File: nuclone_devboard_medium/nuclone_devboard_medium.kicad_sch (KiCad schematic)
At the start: 36 parts, among them J1 JTAG_2X05, J2 TYPE-C-31-M-12, J3 nuclone_medium_left, J4 nuclone_medium_right, SW1 RESET, SW2 Bootloader, U1 MCP1702-MB, U2 TPESD0504C6

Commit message: renamed a library
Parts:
- R1, R13, R2, R3, R4, R5, R6, R7, R8: footprint SquantorRcl:R_0402_hand -> SquantorResistors:R_0402_hand

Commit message: moved RLC parts to different libraries, fixed DRC errors, minor silk movements
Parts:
- added C5: 10n, SquantorCapacitor:C_0402, symbol Device:C
- added R9: 470, SquantorResistor:R_0402_hand, symbol Device:R
- C1, C17, C2: footprint SquantorRcl:C_0603 -> SquantorCapacitor:C_0603
- C14, C4: footprint SquantorRcl:C_0402 -> SquantorCapacitor:C_0402
- C9: footprint SquantorRcl:C_0805 -> SquantorCapacitor:C_0805
- F1: footprint SquantorRcl:F_0603_hand -> SquantorFuse:F_0603_hand
- FB1: footprint SquantorRcl:L_0603 -> SquantorInductor:L_0603
- J2: footprint SquantorUsb:USB-C-HRO-31-M-12 -> SquantorUsb:USB-C-HRO-31-M-12_aisler
- R1, R13, R2, R3, R4, R5, R6, R7, R8: footprint SquantorResistors:R_0402_hand -> SquantorResistor:R_0402_hand
- R14: footprint SquantorRcl:R_0402_hand -> SquantorResistor:R_0402_hand
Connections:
- net VUSB is gone; now on net VBUS: C4.1, U2.5 (VDD)
- net Bootloader: now also C5.1, R9.1; no longer SW2.2
- net DN: now also J2.A7 (DN1), J2.B7 (DN2)
- net DP: now also J2.A6 (DP1), J2.B6 (DP2)
- net VSS: now also C5.2
- new net: R9.2, SW2.2
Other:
- moved on the sheet: SW2

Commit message: updated all footprints, routed and placed, fixed DRC/ERC
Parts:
- C14, C5: value 10n -> 100n; footprint SquantorCapacitor:C_0402 -> SquantorCapacitor:C_0603
- C4: footprint SquantorCapacitor:C_0402 -> SquantorCapacitor:C_0603
- FB1: symbol Device:Ferrite_Bead -> Device:FerriteBead
- N2: value 20211121 -> 20240107
- N5: value Nuclone Template 20211121 -> Nuclone Template 20240107
- R1, R14, R2, R3, R4, R5, R6, R7, R8, R9: footprint SquantorResistor:R_0402_hand -> SquantorResistor:R_0603_hand
- R13: value 100 -> 470; footprint SquantorResistor:R_0402_hand -> SquantorResistor:R_0603_hand
- U1: value MCP1702-MB -> MCP1702-3.3V
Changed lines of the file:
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@@
     )
   )
-  (symbol (lib_id "Device:Ferrite_Bead") (at 63.5 90.17 270) (unit 1)
+  (symbol (lib_id "Device:FerriteBead") (at 63.5 90.17 270) (unit 1)
     (in_bom yes) (on_board yes) (dnp no)
     (property "Reference" "FB1" (at 60.96 87.63 90)
@@
       (effects (font (size 1.524 1.524)) (justify left))
     )
-    (property "Value" "20211121" (at 17.78 182.88 0)
+    (property "Value" "20240107" (at 17.78 182.88 0)
       (effects (font (size 1.524 1.524)) (justify left))
     )
@@
       (effects (font (size 1.524 1.524)))
     )
-    (property "Value" "MCP1702-MB" (at 76.2 181.61 0)
+    (property "Value" "MCP1702-3.3V" (at 76.2 181.61 0)
       (effects (font (size 1.524 1.524)))
     )
@@
       (effects (font (size 1.27 1.27)))
     )
-    (property "Footprint" "SquantorResistor:R_0402_hand" (at 45.72 108.712 90)
+    (property "Footprint" "SquantorResistor:R_0603_hand" (at 45.72 108.712 90)
       (effects (font (size 1.27 1.27)) hide)
     )
@@
       (effects (font (size 1.27 1.27)))
     )
-    (property "Footprint" "SquantorResistor:R_0402_hand" (at 25.4 132.842 90)
+    (property "Footprint" "SquantorResistor:R_0603_hand" (at 25.4 132.842 90)
       (effects (font (size 1.27 1.27)) hide)
     )
@@
       (effects (font (size 1.27 1.27)))
     )
-    (property "Footprint" "SquantorResistor:R_0402_hand" (at 25.4 135.382 90)
+    (property "Footprint" "SquantorResistor:R_0603_hand" (at 25.4 135.382 90)
       (effects (font (size 1.27 1.27)) hide)
     )
@@
       (effects (font (size 1.27 1.27)))
     )
-    (property "Footprint" "SquantorResistor:R_0402_hand" (at 25.4 137.922 90)
+    (property "Footprint" "SquantorResistor:R_0603_hand" (at 25.4 137.922 90)
       (effects (font (size 1.27 1.27)) hide)
     )
@@
       (effects (font (size 1.27 1.27)))
     )
-    (property "Footprint" "SquantorResistor:R_0402_hand" (at 25.4 140.462 90)
+    (property "Footprint" "SquantorResistor:R_0603_hand" (at 25.4 140.462 90)
       (effects (font (size 1.27 1.27)) hide)
     )
@@
       (effects (font (size 1.27 1.27)))
     )
-    (property "Footprint" "SquantorResistor:R_0402_hand" (at 25.4 143.002 90)
+    (property "Footprint" "SquantorResistor:R_0603_hand" (at 25.4 143.002 90)
       (effects (font (size 1.27 1.27)) hide)
     )
@@
       (effects (font (size 1.27 1.27)))
     )
-    (property "Value" "100" (at 43.18 152.4 90)
-      (effects (font (size 1.27 1.27)))
-    )
-    (property "Footprint" "SquantorResistor:R_0402_hand" (at 43.18 150.622 90)
+    (property "Value" "470" (at 43.18 152.4 90)
+      (effects (font (size 1.27 1.27)))
+    )
+    (property "Footprint" "SquantorResistor:R_0603_hand" (at 43.18 150.622 90)
       (effects (font (size 1.27 1.27)) hide)
     )
@@
       (effects (font (size 1.27 1.27)))
     )
-    (property "Value" "10n" (at 58.42 151.13 90)
-      (effects (font (size 1.27 1.27)))
-    )
-    (property "Footprint" "SquantorCapacitor:C_0402" (at 50.8 153.3652 0)
+    (property "Value" "100n" (at 58.42 151.13 90)
+      (effects (font (size 1.27 1.27)))
+    )
+    (property "Footprint" "SquantorCapacitor:C_0603" (at 50.8 153.3652 0)
       (effects (font (size 1.27 1.27)) hide)
     )
@@
       (effects (font (size 1.27 1.27)))
     )
-    (property "Footprint" "SquantorResistor:R_0402_hand" (at 81.28 188.468 90)
+    (property "Footprint" "SquantorResistor:R_0603_hand" (at 81.28 188.468 90)
       (effects (font (size 1.27 1.27)) hide)
     )
@@
       (effects (font (size 1.27 1.27)))
     )
-    (property "Footprint" "SquantorResistor:R_0402_hand" (at 45.72 93.472 90)
+    (property "Footprint" "SquantorResistor:R_0603_hand" (at 45.72 93.472 90)
       (effects (font (size 1.27 1.27)) hide)
     )
@@
       (effects (font (size 1.27 1.27)))
     )
-    (property "Footprint" "SquantorResistor:R_0402_hand" (at 90.17 141.732 90)
+    (property "Footprint" "SquantorResistor:R_0603_hand" (at 90.17 141.732 90)
       (effects (font (size 1.27 1.27)) hide)
     )
@@
       (effects (font (size 1.524 1.524)) (justify left))
     )
-    (property "Value" "Nuclone Template 20211121" (at 20.32 163.83 0)
+    (property "Value" "Nuclone Template 20240107" (at 20.32 163.83 0)
       (effects (font (size 1.524 1.524)) (justify left))
     )
@@
       (effects (font (size 1.27 1.27)))
     )
-    (property "Footprint" "SquantorResistor:R_0402_hand" (at 100.33 131.572 90)
+    (property "Footprint" "SquantorResistor:R_0603_hand" (at 100.33 131.572 90)
       (effects (font (size 1.27 1.27)) hide)
     )
@@
       (effects (font (size 1.27 1.27)))
     )
-    (property "Footprint" "SquantorCapacitor:C_0402" (at 64.77 120.3452 0)
+    (property "Footprint" "SquantorCapacitor:C_0603" (at 64.77 120.3452 0)
       (effects (font (size 1.27 1.27)) hide)
     )
@@
       (effects (font (size 1.27 1.27)))
     )
-    (property "Value" "10n" (at 93.98 137.16 90)
-      (effects (font (size 1.27 1.27)))
-    )
-    (property "Footprint" "SquantorCapacitor:C_0402" (at 86.36 139.3952 0)
-      (effects (font (size 1.27 1.27)) hide)
-    )
+    (property "Value" "100n" (at 93.98 137.16 90)
+      (effects (font (size 1.27 1.27)))
+    )
+    (property "Footprint" "SquantorCapacitor:C_0603" (at 86.36 139.3952 0)
+      (effects (font (size 1.27 1.27)) hide)
+    )

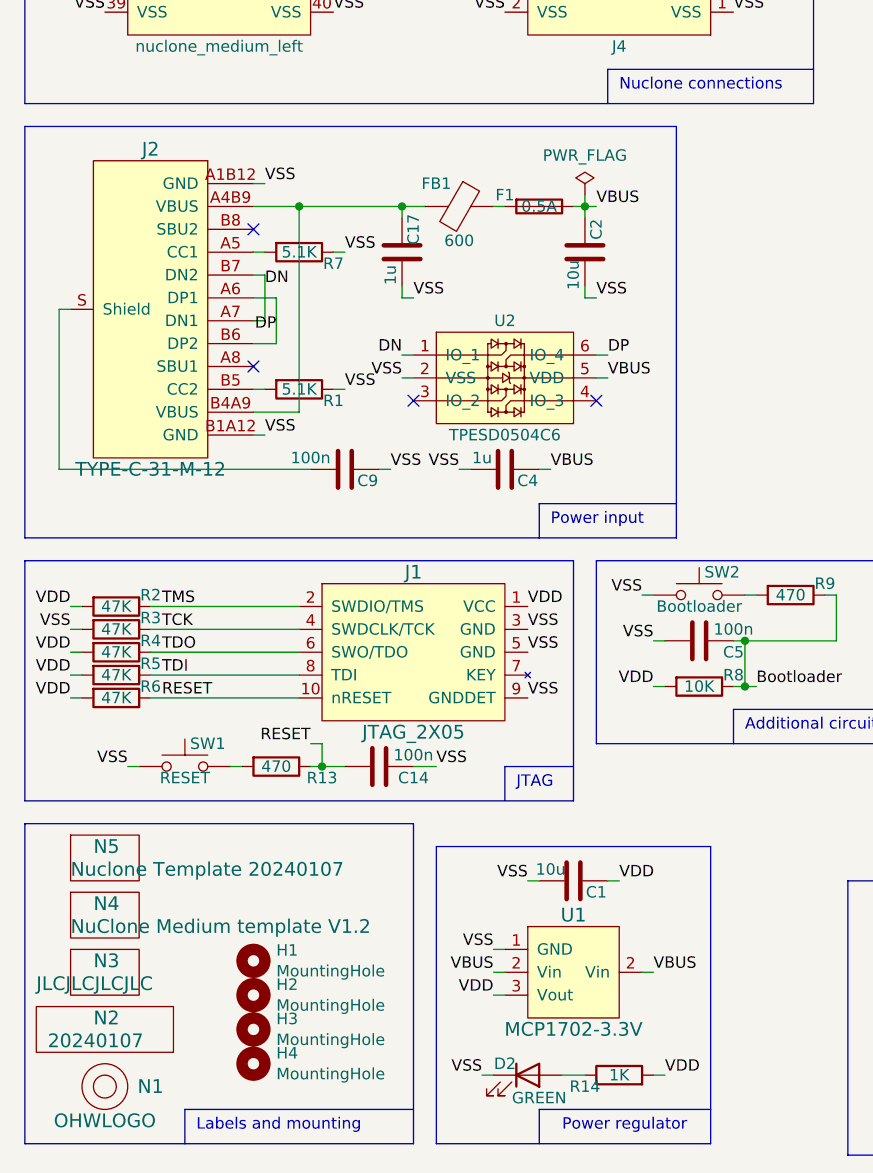
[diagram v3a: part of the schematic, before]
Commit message: trace optimizations
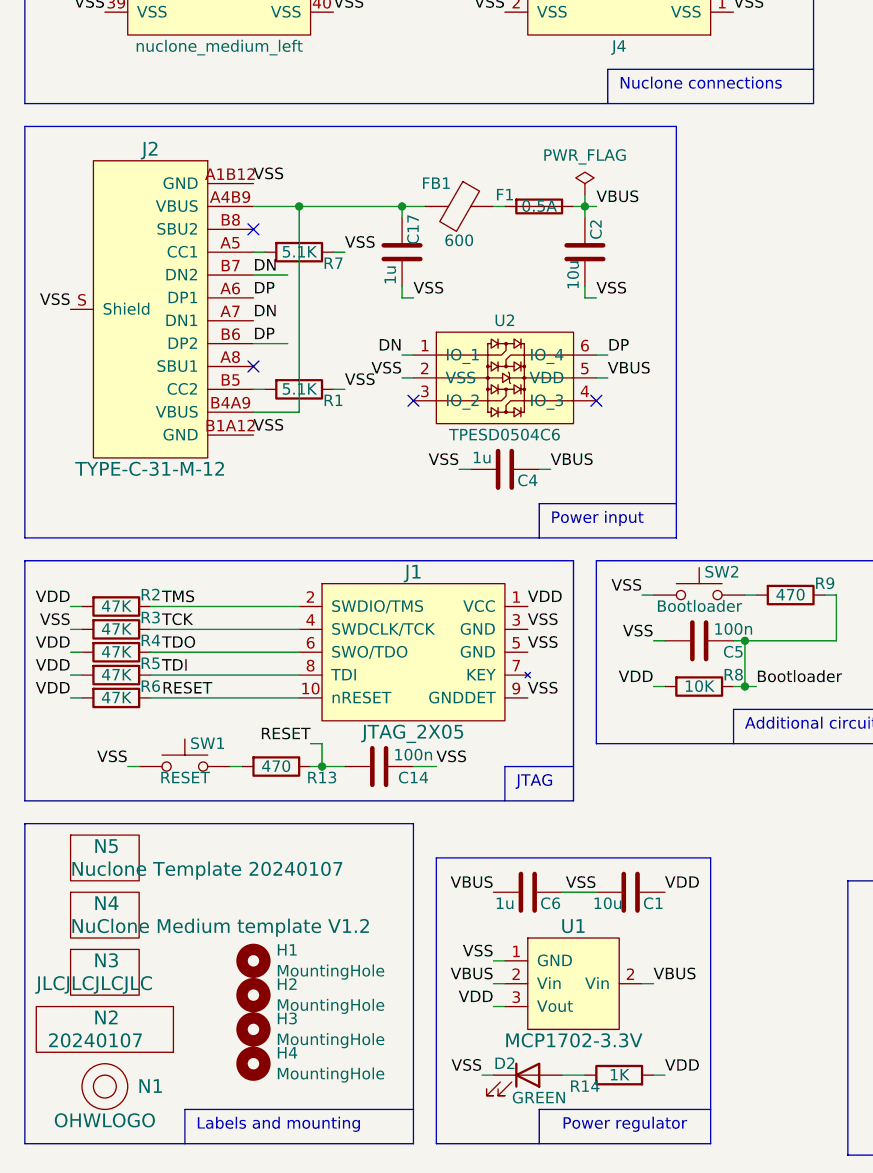
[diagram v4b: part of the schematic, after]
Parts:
- removed C9: 100n, SquantorCapacitor:C_0805, symbol Device:C
- added C6: 1u, SquantorCapacitor:C_0603, symbol Device:C
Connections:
- net VBUS: now also C6.2
- net VSS: now also J2.S (Shield), C6.1
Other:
- moved on the sheet: C1, U1

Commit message: updated versionnumbers
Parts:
- N2: value 20240107 -> V20240114; footprint SquantorLabels:Label_version -> SquantorLabels:Label_Generic
- N4: value NuClone Medium template V1.2 -> NuClone Medium template V1.3
- N5: value Nuclone Template 20240107 -> Nuclone Template V20240114
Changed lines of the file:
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@@
       (effects (font (size 1.524 1.524)) (justify left))
     )
-    (property "Value" "20240107" (at 17.78 182.88 0)
-      (effects (font (size 1.524 1.524)) (justify left))
-    )
-    (property "Footprint" "SquantorLabels:Label_version" (at 24.13 182.88 0)
+    (property "Value" "V20240114" (at 17.78 182.88 0)
+      (effects (font (size 1.524 1.524)) (justify left))
+    )
+    (property "Footprint" "SquantorLabels:Label_Generic" (at 24.13 182.88 0)
       (effects (font (size 1.524 1.524)) hide)
     )
@@
       (effects (font (size 1.524 1.524)) (justify left))
     )
-    (property "Value" "NuClone Medium template V1.2" (at 20.32 170.18 0)
+    (property "Value" "NuClone Medium template V1.3" (at 20.32 170.18 0)
       (effects (font (size 1.524 1.524)) (justify left))
     )
@@
       (effects (font (size 1.524 1.524)) (justify left))
     )
-    (property "Value" "Nuclone Template 20240107" (at 20.32 163.83 0)
-      (effects (font (size 1.524 1.524)) (justify left))
-    )
+    (property "Value" "Nuclone Template V20240114" (at 20.32 163.83 0)
+      (effects (font (size 1.524 1.524)) (justify left))
+    )
